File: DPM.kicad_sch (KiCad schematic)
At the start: 13 parts, among them U1 74HC590A, U2 74HC682

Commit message: git-svn-id: file:///D%5C00%20-%20Dev%20&%20Calculs%5CRepoTortoiseSVN_PCB%5CD-DPM/trunk@9 f29d8339-a183-0348-962e-9e4594cf8312
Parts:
- removed U1: 74HC590A, Package_DIP:DIP-16_W7.62mm_Socket_LongPads, symbol 74xx:74HC590A
- added U1: 74HC590, Package_DIP:DIP-16_W7.62mm_Socket_LongPads, symbol Perso_Spare_parts:74HC590
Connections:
- net GND: now also U1.12 (~{CCKEN}), U1.8 (GND)
- net VCC: now also U2.20 (VCC), U1.16 (VCC)
- net at U2.11 (P4): now also U1.3 (Q3)
- net at U2.13 (P5): now also U1.2 (Q2)
- net at U2.15 (P6): now also U1.1 (Q1)
- net at U2.17 (P7): now also U1.15 (Q0)
- net at U2.2 (P0): now also U1.7 (Q7)
- net at U2.4 (P1): now also U1.6 (Q6)
- net at U2.6 (P2): now also U1.5 (Q5)
- net at U2.8 (P3): now also U1.4 (Q4)
- no-connect marks 12 -> 13

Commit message: git-svn-id: file:///D%5C00%20-%20Dev%20&%20Calculs%5CRepoTortoiseSVN_PCB%5CD-DPM/trunk@12 f29d8339-a183-0348-962e-9e4594cf8312
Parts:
- added J1: Conn_01x08, Connector_PinHeader_2.54mm:PinHeader_1x08_P2.54mm_Vertical, symbol Connector_Generic:Conn_01x08
- added U4: MCP23017_SP, Package_DIP:DIP-28_W7.62mm_Socket_LongPads, symbol Interface_Expansion:MCP23017_SP
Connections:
- net GND: now also U1.14 (~{OE}), U4.10 (VSS)
- net VCC: now also U1.10 (~{CCLR}), U4.18 (~{RESET}), U4.9 (VDD)
- net Clock: now reaches U1.11 (CCLK)
- net Clock: now also U1.13 (RCLK)
- net at U2.1 (~{P>Q}): now also J1.1 (Pin_1)
- net at U2.12 (Q4): now also U4.5 (GPB4)
- net at U2.14 (Q5): now also U4.6 (GPB5)
- net at U2.16 (Q6): now also U4.7 (GPB6)
- net at U2.18 (Q7): now also U4.8 (GPB7)
- net at U2.3 (Q0): now also U4.1 (GPB0)
- net at U2.5 (Q1): now also U4.2 (GPB1)
- net at U2.7 (Q2): now also U4.3 (GPB2)
- net at U2.9 (Q3): now also U4.4 (GPB3)
- new net: J1.6 (Pin_6), U4.15 (A0)
- new net: J1.7 (Pin_7), U4.16 (A1)
- new net: J1.8 (Pin_8), U4.17 (A2)
- new net SCL: U4.12 (SCK)
- new net SDA: U4.13 (SDA)
- no-connect marks 13 -> 30
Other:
- moved on the sheet: C_1, C_2, F1, H1, H2, H3, H4, J_VIN_0, LDL1, LED1, R5, U1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

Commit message: DPM et DDPM implémentés Mouais bof pour ajouter ma DPM en code Gray
Sinon OK Tiers pour en faire la branche 1

git-svn-id: file:///D%5C00%20-%20Dev%20&%20Calculs%5CRepoTortoiseSVN_PCB%5CD-DPM/trunk@14 f29d8339-a183-0348-962e-9e4594cf8312
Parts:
- added U3, U5: ADG333A, Package_DIP:DIP-20_W7.62mm_Socket_LongPads, symbol Perso_Spare_parts:ADG333A
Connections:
- net GND: now also U3.15 (NC), U3.17 (S4B), U3.5 (Vss), U3.6 (GND), U5.15 (NC), U5.5 (Vss), U5.6 (GND)
- net VCC: now also U3.16 (VDD), U5.16 (VDD)
- net DPM: now reaches J1.1 (Pin_1), U2.1 (~{P>Q})
- net Dyadic DPM: now reaches J1.2 (Pin_2)
- net Dyadic DPM: now also U5.3 (D1)
- net Gray DPM: now reaches J1.3 (Pin_3)
- net I2C_A0: now reaches U4.15 (A0)
- net I2C_A0: now also J1.8 (Pin_8); no longer J1.6 (Pin_6)
- net I2C_A1: now reaches J1.7 (Pin_7), U4.16 (A1)
- net I2C_A2: now reaches U4.17 (A2)
- net I2C_A2: now also J1.6 (Pin_6); no longer J1.8 (Pin_8)
- net Q1: now reaches U1.1 (Q1), U2.15 (P6)
- net Q1: now also U5.20 (IN4)
- net Q0: now reaches U1.15 (Q0), U2.17 (P7)
- net Q0: now also U5.1 (IN1)
- net Q2: now reaches U1.2 (Q2), U2.13 (P5)
- net Q2: now also U5.11 (IN3)
- net Q3: now reaches U1.3 (Q3), U2.11 (P4)
- net Q3: now also U5.10 (IN2)
- net Q4: now reaches U1.4 (Q4), U2.8 (P3)
- net Q4: now also U3.11 (IN3)
- net Q5: now reaches U1.5 (Q5), U2.6 (P2)
- net Q5: now also U3.10 (IN2)
- net Q6: now reaches U1.6 (Q6), U2.4 (P1)
- net Q6: now also U3.1 (IN1)
- net Q7: now reaches U1.7 (Q7), U2.2 (P0)
- net Q7: now also U3.20 (IN4)
- net at U4.1 (GPB0): no longer U2.3 (Q0)
- net at U4.2 (GPB1): no longer U2.5 (Q1)
- net B0: now reaches U4.21 (GPA0)
- net B0: now also U2.3 (Q0), U3.19 (S4A)
- net B1: now reaches U4.22 (GPA1)
- net B1: now also U2.5 (Q1), U3.2 (S1A)
- net B2: now reaches U4.23 (GPA2)
- net B2: now also U2.7 (Q2), U3.9 (S2A)
- net B3: now reaches U4.24 (GPA3)
- net B3: now also U2.9 (Q3), U3.12 (S3A)
- net B4: now reaches U4.25 (GPA4)
- net B4: now also U2.12 (Q4), U5.9 (S2A)
- net B5: now reaches U4.26 (GPA5)
- net B5: now also U2.14 (Q5), U5.12 (S3A)
- net B6: now reaches U4.27 (GPA6)
- net B6: now also U2.16 (Q6), U5.19 (S4A)
- net B7: now reaches U4.28 (GPA7)
- net B7: now also U2.18 (Q7), U5.2 (S1A)
- net at U4.3 (GPB2): no longer U2.7 (Q2)
- net at U4.4 (GPB3): no longer U2.9 (Q3)
- net at U4.5 (GPB4): no longer U2.12 (Q4)
- net at U4.6 (GPB5): no longer U2.14 (Q5)
- net at U4.7 (GPB6): no longer U2.16 (Q6)
- net at U4.8 (GPB7): no longer U2.18 (Q7)
- new net: U5.13 (D3), U5.17 (S4B)
- new net: U5.14 (S3B), U5.8 (D2)
- new net: U5.18 (D4), U5.4 (S1B)
- new net: U3.13 (D3), U5.7 (S2B)
- new net: U3.14 (S3B), U3.8 (D2)
- new net: U3.18 (D4), U3.4 (S1B)
- new net: U3.3 (D1), U3.7 (S2B)
- no-connect marks 30 -> 28
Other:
- moved on the sheet: J1, U1, U2, U4

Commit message: - Ajout de screenshots de doc
git-svn-id: file:///D%5C00%20-%20Dev%20&%20Calculs%5CRepoTortoiseSVN_PCB%5CD-DPM/trunk@15 f29d8339-a183-0348-962e-9e4594cf8312
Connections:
- net B0: now also U4.1 (GPB0); no longer U2.3 (Q0), U4.21 (GPA0)
- net B1: now also U4.2 (GPB1); no longer U2.5 (Q1), U4.22 (GPA1)
- net B2: now also U4.3 (GPB2); no longer U2.7 (Q2), U4.23 (GPA2)
- net B3: now also U4.4 (GPB3); no longer U2.9 (Q3), U4.24 (GPA3)
- net B4: now also U4.5 (GPB4); no longer U2.12 (Q4), U4.25 (GPA4)
- net B5: now also U4.6 (GPB5); no longer U2.14 (Q5), U4.26 (GPA5)
- net B6: now also U4.7 (GPB6); no longer U2.16 (Q6), U4.27 (GPA6)
- net B7: now also U4.8 (GPB7); no longer U2.18 (Q7), U4.28 (GPA7)
- new net: U2.3 (Q0), U4.21 (GPA0)
- new net: U2.5 (Q1), U4.22 (GPA1)
- new net: U2.7 (Q2), U4.23 (GPA2)
- new net: U2.9 (Q3), U4.24 (GPA3)
- new net: U2.12 (Q4), U4.25 (GPA4)
- new net: U2.14 (Q5), U4.26 (GPA5)
- new net: U2.16 (Q6), U4.27 (GPA6)
- new net: U2.18 (Q7), U4.28 (GPA7)
- no-connect marks 28 -> 23
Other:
- moved on the sheet: U1, U2, U3, U4, U5

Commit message: + 3 fonctionnalités : PWM, DPM & DDPM + début du routage de la carte
git-svn-id: file:///D%5C00%20-%20Dev%20&%20Calculs%5CRepoTortoiseSVN_PCB%5CD-DPM/trunk@16 f29d8339-a183-0348-962e-9e4594cf8312
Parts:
- removed J1: Conn_01x08, Connector_PinHeader_2.54mm:PinHeader_1x08_P2.54mm_Vertical, symbol Connector_Generic:Conn_01x08
- removed U1: 74HC590, Package_DIP:DIP-16_W7.62mm_Socket_LongPads, symbol Perso_Spare_parts:74HC590
- removed U2: 74HC682, Package_DIP:DIP-20_W7.62mm_Socket_LongPads, symbol Perso_Spare_parts:74HC682
- added J1: Conn_02x12_Odd_Even, Connector_PinHeader_2.54mm:PinHeader_2x12_P2.54mm_Vertical, symbol Connector_Generic:Conn_02x12_Odd_Even
- added JP1, JP2, JP3: Jumper_3_Open, Connector_PinHeader_2.54mm:PinHeader_1x03_P2.54mm_Vertical, symbol Jumper:Jumper_3_Open
- added JP4: JTAG-X, Connector_IDC:IDC-Header_2x07_P2.54mm_Horizontal, symbol Connector_Generic:Conn_02x07_Odd_Even
- added U25, U28, U31: 74LS85, Package_DIP:DIP-16_W7.62mm_Socket, symbol 74xx:74LS85
- added U6: ADG333A, Package_DIP:DIP-20_W7.62mm_Socket_LongPads, symbol Perso_Spare_parts:ADG333A
- added U8: 4040, Package_DIP:DIP-16_W7.62mm_Socket, symbol 4xxx:4040
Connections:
- net Clock: now also U8.10 (CLK)
- net DPM: now also U31.7 (Oa<b), U6.13 (D3)
- net GND: now also JP1.1 (A), JP2.1 (A), JP3.1 (A), U25.2 (Ia<b), U25.4 (Ia>b), U25.8 (GND), U28.8 (GND), U31.8 (GND), U6.15 (NC), U6.5 (Vss), U6.6 (GND), U8.8 (VSS)
- net Q0: now also J1.1 (Pin_1), U8.9 (Q0); no longer U5.1 (IN1)
- net Q1: now also J1.5 (Pin_5), U8.7 (Q1); no longer U5.20 (IN4)
- net Q2: now also J1.9 (Pin_9), U8.6 (Q2); no longer U5.11 (IN3)
- net Q3: now also J1.13 (Pin_13), U8.5 (Q3); no longer U5.10 (IN2)
- net Q4: now also J1.20 (Pin_20), U8.3 (Q4); no longer U3.11 (IN3)
- net Q5: now also J1.21 (Pin_21), U8.2 (Q5); no longer U3.10 (IN2)
- net Q6: now also J1.24 (Pin_24), U8.4 (Q6); no longer U3.1 (IN1)
- net Q7: now also J1.17 (Pin_17), U8.13 (Q7); no longer U3.20 (IN4)
- net VCC: now also JP1.3 (B), JP2.3 (B), JP3.3 (B), U25.16 (VCC), U25.3 (Ia=b), U28.16 (VCC), U31.16 (VCC), U6.16 (VDD), U8.16 (VDD); no longer U4.18 (~{RESET})
- net A0: now reaches U4.21 (GPA0)
- net A0: now also U3.19 (S4A), U25.9 (B0)
- net A1: now reaches U4.22 (GPA1)
- net A1: now also U3.2 (S1A), U25.11 (B1)
- net A2: now reaches U4.23 (GPA2)
- net A2: now also U3.9 (S2A), U25.14 (B2)
- net A3: now reaches U4.24 (GPA3)
- net A3: now also U3.12 (S3A), U25.1 (B3)
- net A4: now reaches U4.25 (GPA4)
- net A4: now also U5.19 (S4A), U28.9 (B0)
- net A5: now reaches U4.26 (GPA5)
- net A5: now also U5.2 (S1A), U28.11 (B1)
- net A6: now reaches U4.27 (GPA6)
- net A6: now also U5.9 (S2A), U28.14 (B2)
- net A7: now reaches U4.28 (GPA7)
- net A7: now also U5.12 (S3A), U28.1 (B3)
- net at U5.13 (D3): now also U6.17 (S4B); no longer U5.17 (S4B)
- net at U3.13 (D3): now also U5.17 (S4B); no longer U5.7 (S2B)
- net B0 renamed A8
- net A8: now also U31.9 (B0), U6.19 (S4A); no longer U3.19 (S4A)
- net B1 renamed A9
- net A9: now also U31.11 (B1), U6.2 (S1A); no longer U3.2 (S1A)
- net B2 renamed A10
- net A10: now also U31.14 (B2), U6.9 (S2A); no longer U3.9 (S2A)
- net B3 renamed A11
- net A11: now also U31.1 (B3), U6.12 (S3A); no longer U3.12 (S3A)
- net B4 renamed PreScaler0
- net PreScaler0: no longer U5.9 (S2A)
- net B5 renamed PreScaler1
- net PreScaler1: no longer U5.12 (S3A)
- net B6 renamed PreScaler2
- net PreScaler2: no longer U5.19 (S4A)
- net B7 renamed ~{CntEN}
- net ~{CntEN}: now also U8.11 (Reset); no longer U5.2 (S1A)
- net Dyadic DPM: no longer names the net of U5.3 (D1)
- net Dyadic DPM: now also U5.7 (S2B)
- net I2C_A0: no longer names the net of U4.15 (A0)
- net I2C_A0: now also JP3.2 (C)
- net I2C_A1: no longer names the net of U4.16 (A1)
- net I2C_A1: now also JP2.2 (C)
- net I2C_A2: no longer names the net of U4.17 (A2)
- net I2C_A2: now also JP1.2 (C)
- new net: U6.14 (S3B), U6.8 (D2)
- new net: U6.18 (D4), U6.4 (S1B)
- new net: U6.3 (D1), U6.7 (S2B)
- new net: U25.7 (Oa<b), U28.2 (Ia<b)
- new net: U25.6 (Oa=b), U28.3 (Ia=b)
- new net: U25.5 (Oa>b), U28.4 (Ia>b)
- new net: U28.5 (Oa>b), U31.4 (Ia>b)
- new net: U28.6 (Oa=b), U31.3 (Ia=b)
- new net: U28.7 (Oa<b), U31.2 (Ia<b)
- new net CNT_A0: J1.2 (Pin_2), U25.10 (A0)
- new net CNT_A1: J1.6 (Pin_6), U25.12 (A1)
- new net CNT_A10: J1.7 (Pin_7), U31.13 (A2)
- new net CNT_A11: J1.3 (Pin_3), U31.15 (A3)
- new net CNT_A2: J1.10 (Pin_10), U25.13 (A2)
- new net CNT_A3: J1.14 (Pin_14), U25.15 (A3)
- new net CNT_A4: J1.19 (Pin_19), U28.10 (A0)
- new net CNT_A5: J1.22 (Pin_22), U28.12 (A1)
- new net CNT_A6: J1.23 (Pin_23), U28.13 (A2)
- new net CNT_A7: J1.18 (Pin_18), U28.15 (A3)
- new net CNT_A8: J1.15 (Pin_15), U31.10 (A0)
- new net CNT_A9: J1.11 (Pin_11), U31.12 (A1)
- new net Q10: J1.8 (Pin_8), U8.15 (Q10)
- new net Q11: J1.4 (Pin_4), U8.1 (Q11)
- new net Q8: J1.16 (Pin_16), U8.12 (Q8)
- new net Q9: J1.12 (Pin_12), U8.14 (Q9)
- new net ~{Reset}: U4.18 (~{RESET})
- no-connect marks 23 -> 20
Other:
- moved on the sheet: U3, U4

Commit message: POPOPO !!!!! 1ere version du routage de la carte
git-svn-id: file:///D%5C00%20-%20Dev%20&%20Calculs%5CRepoTortoiseSVN_PCB%5CD-DPM/trunk@17 f29d8339-a183-0348-962e-9e4594cf8312
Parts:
- JP4: value JTAG-X -> IDC-14
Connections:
- net VCC is gone; now on net +5V: C_2.2, JP1.3 (B), JP2.3 (B), JP3.3 (B), LDL1.2 (VO), R5.1, U25.16 (VCC), U25.3 (Ia=b), U28.16 (VCC), U3.16 (VDD), U31.16 (VCC), U4.9 (VDD), U5.16 (VDD), U6.16 (VDD), U8.16 (VDD)
- net Clock: now also JP4.10 (Pin_10)
- net GND: now also JP4.3 (Pin_3), JP4.4 (Pin_4)
- net SCL: now also JP4.14 (Pin_14)
- net SDA: now also JP4.12 (Pin_12)
- net VBatt: now also JP4.2 (Pin_2)
- net ~{Reset}: now also JP4.8 (Pin_8)
- net +5V: now reaches JP4.1 (Pin_1)
- no-connect marks 20 -> 10
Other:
- removed sheet Connection PCI CAN Express
- moved on the sheet: JP4

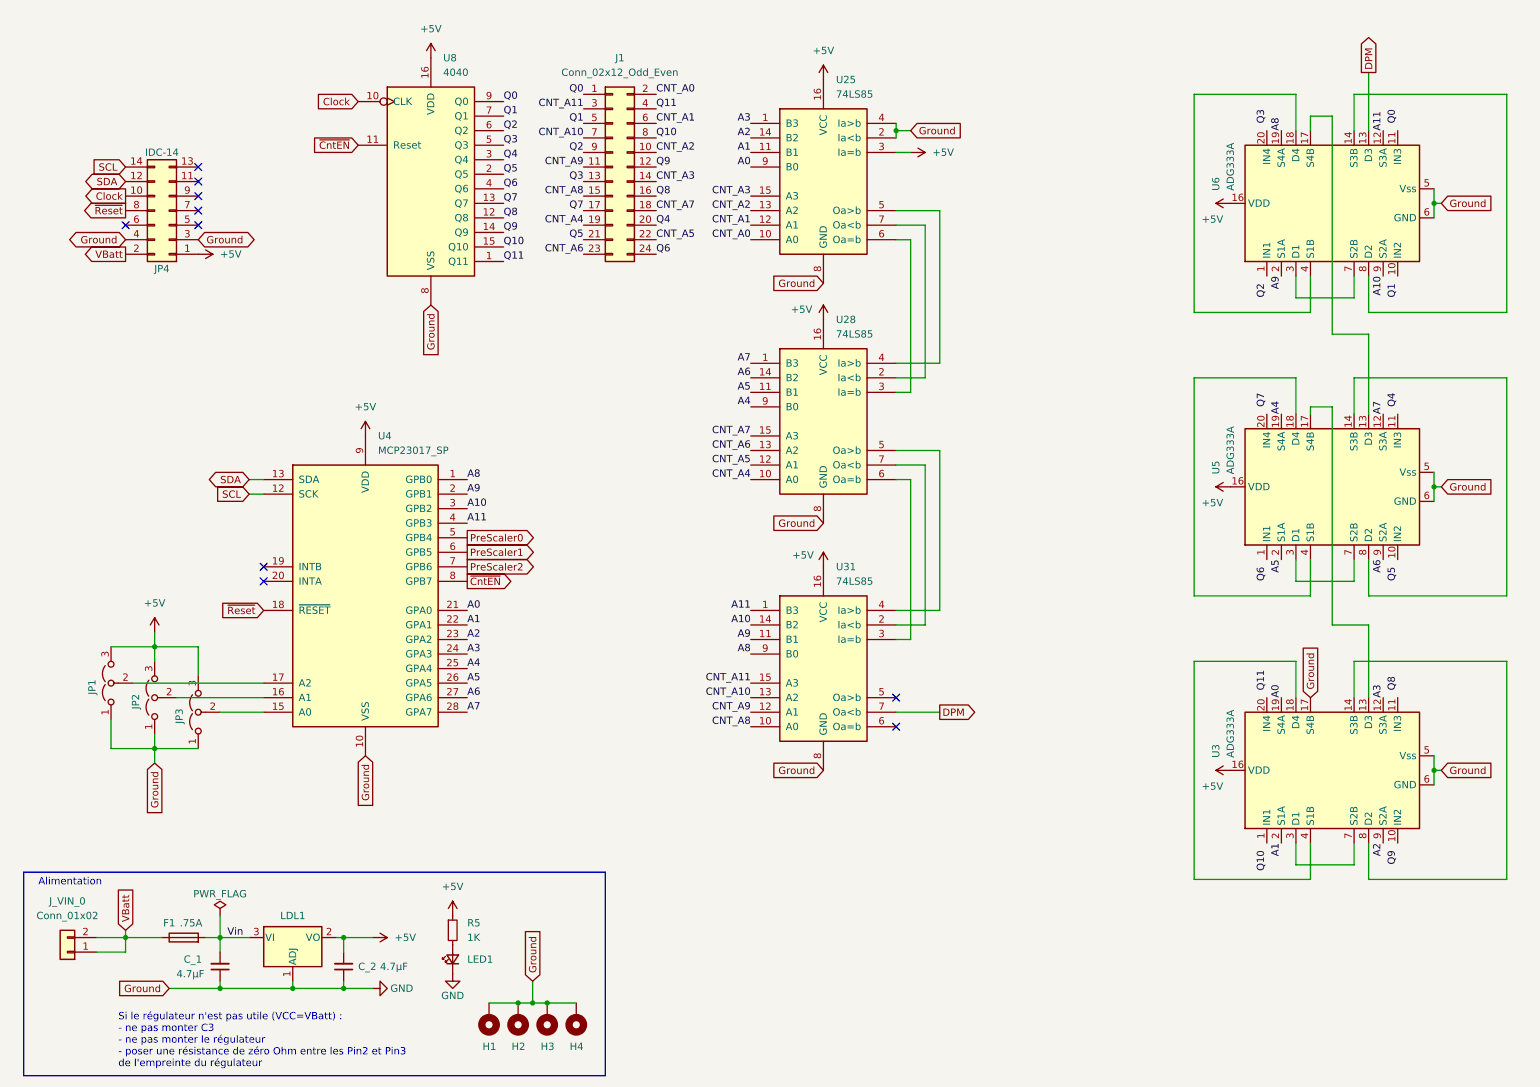
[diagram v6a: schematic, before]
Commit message: Ajout du prescaler TODO : - condensateurs de découplage - bouchon I2C
git-svn-id: file:///D%5C00%20-%20Dev%20&%20Calculs%5CRepoTortoiseSVN_PCB%5CD-DPM/trunk@18 f29d8339-a183-0348-962e-9e4594cf8312
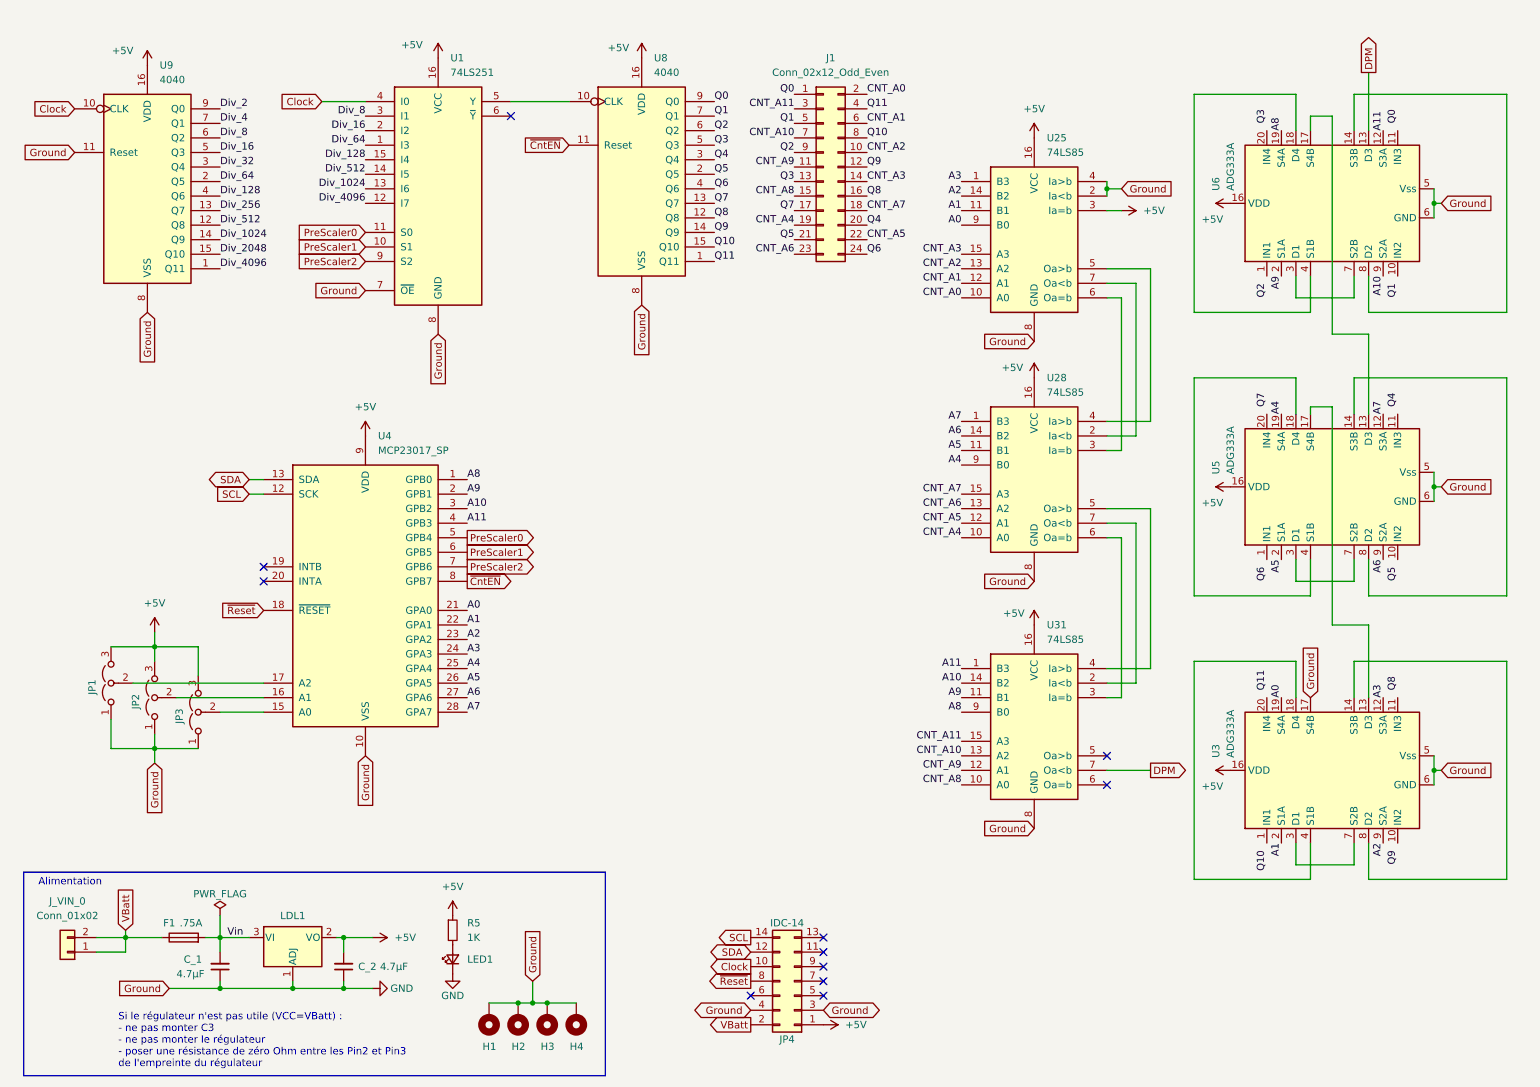
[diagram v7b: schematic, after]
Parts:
- added U1: 74LS251, Package_DIP:DIP-16_W7.62mm_Socket, symbol 74xx:74LS251
- added U9: 4040, Package_DIP:DIP-16_W7.62mm_Socket, symbol 4xxx:4040
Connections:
- net +5V: now also U1.16 (VCC), U9.16 (VDD)
- net Clock: now also U1.4 (I0), U9.10 (CLK); no longer U8.10 (CLK)
- net GND: now also U1.7 (~{OE}), U1.8 (GND), U9.11 (Reset), U9.8 (VSS)
- net PreScaler0: now also U1.11 (S0)
- net PreScaler1: now also U1.10 (S1)
- net PreScaler2: now also U1.9 (S2)
- new net: U1.5 (Y), U8.10 (CLK)
- new net Div_1024: U1.13 (I6), U9.14 (Q9)
- new net Div_128: U1.15 (I4), U9.4 (Q6)
- new net Div_16: U1.2 (I2), U9.5 (Q3)
- new net Div_2: U9.9 (Q0)
- new net Div_2048: U9.15 (Q10)
- new net Div_256: U9.13 (Q7)
- new net Div_32: U9.3 (Q4)
- new net Div_4: U9.7 (Q1)
- new net Div_4096: U1.12 (I7), U9.1 (Q11)
- new net Div_512: U1.14 (I5), U9.12 (Q8)
- new net Div_64: U1.1 (I3), U9.2 (Q5)
- new net Div_8: U1.3 (I1), U9.6 (Q2)
- no-connect marks 10 -> 11
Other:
- moved on the sheet: J1, JP4, U25, U28, U31, U8
